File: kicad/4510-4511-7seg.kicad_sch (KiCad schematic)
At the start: 14 parts, among them U13 4029, U14 4511, U15 TDSR-3163-G

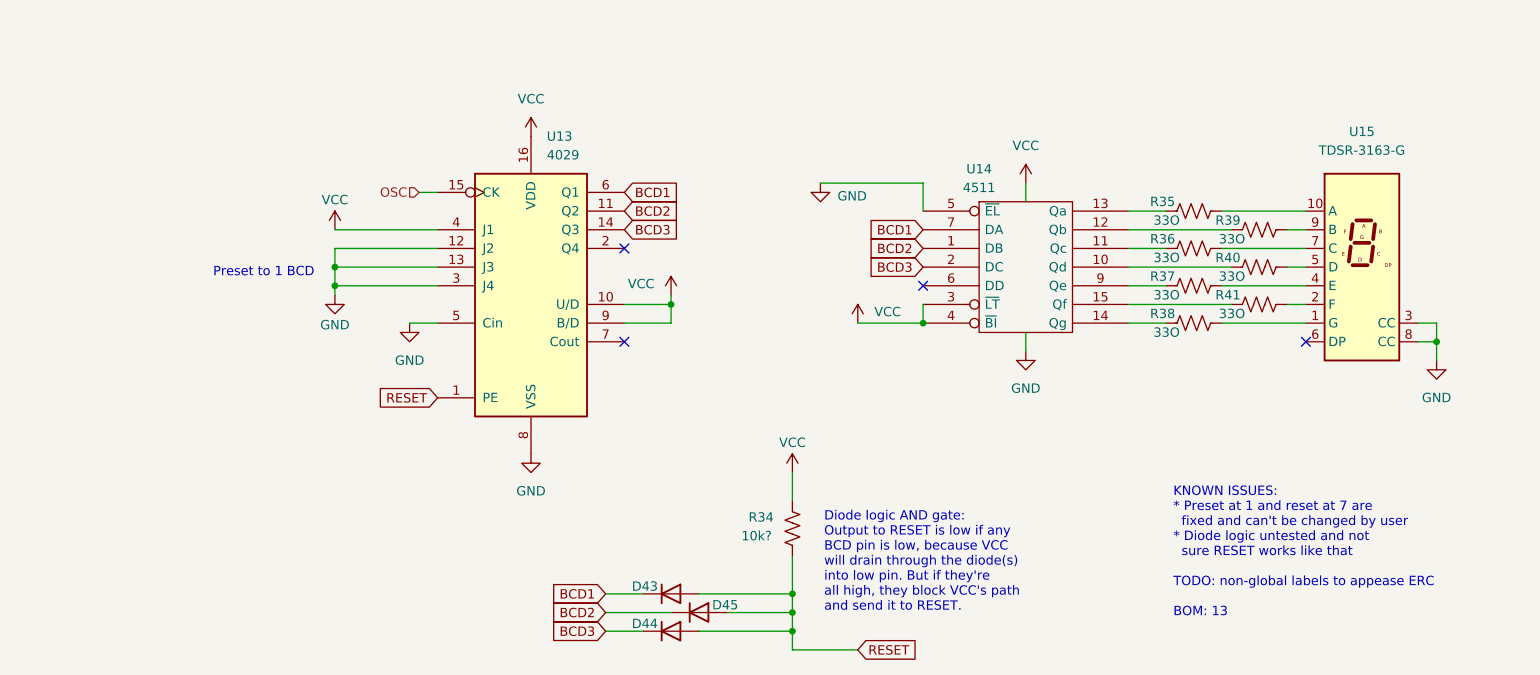
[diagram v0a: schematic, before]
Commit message: Add CD4510 to CD4511 to 7seg schematic
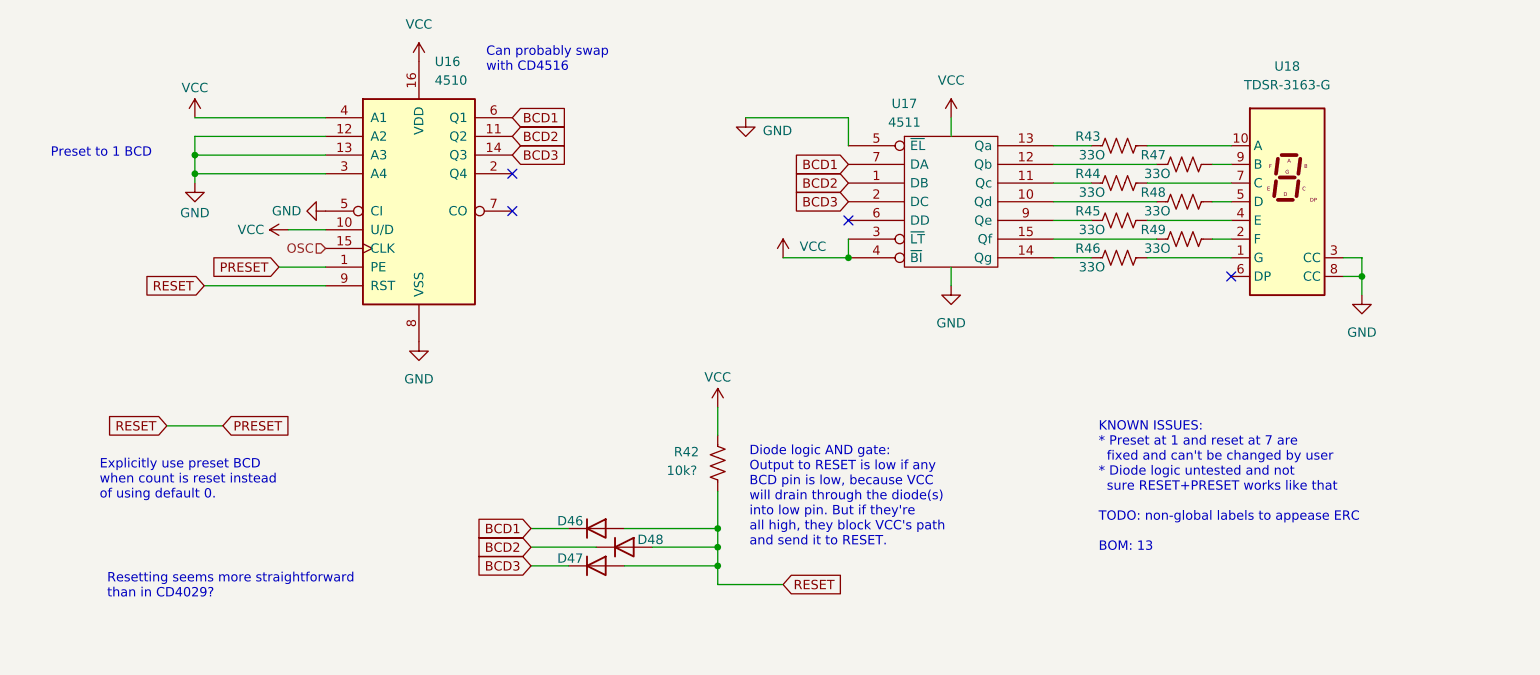
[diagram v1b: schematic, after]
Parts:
- removed D43, D44, D45: 1N4148WT, Diode_SMD:D_SOD-523, symbol Diode:1N4148WT
- removed R34: 10k?, Resistor_THT:R_Axial_DIN0204_L3.6mm_D1.6mm_P7.62mm_Horizontal, symbol Device:R_US
- removed R35, R36, R37, R38, R39, R40, R41: 33O, Resistor_THT:R_Axial_DIN0204_L3.6mm_D1.6mm_P7.62mm_Horizontal, symbol Device:R_US
- removed U13: 4029, symbol 4xxx:4029
- removed U14: 4511, symbol 4xxx_IEEE:4511
- removed U15: TDSR-3163-G, symbol parts_cafe:TDSR-3163-G
- added D46, D47, D48: 1N4148WT, Diode_SMD:D_SOD-523, symbol Diode:1N4148WT
- added R42: 10k?, Resistor_THT:R_Axial_DIN0204_L3.6mm_D1.6mm_P7.62mm_Horizontal, symbol Device:R_US
- added R43, R44, R45, R46, R47, R48, R49: 33O, Resistor_THT:R_Axial_DIN0204_L3.6mm_D1.6mm_P7.62mm_Horizontal, symbol Device:R_US
- added U16: 4510, symbol 4xxx:4510
- added U17: 4511, symbol 4xxx_IEEE:4511
- added U18: TDSR-3163-G, symbol parts_cafe:TDSR-3163-G
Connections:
- net BCD1: now also D46.1 (K), U16.6 (Q1), U17.7 (DA)
- net BCD2: now also D48.1 (K), U16.11 (Q2), U17.1 (DB)
- net BCD3: now also D47.1 (K), U16.14 (Q3), U17.2 (DC)
- net GND: now also U16.12 (A2), U16.13 (A3), U16.3 (A4), U16.5 (CI), U16.8 (VSS), U17.5 (~{EL}), U17.8 (Vss), U18.3 (CC), U18.8 (CC)
- net OSC: now also U16.15 (CLK)
- net VCC: now also R42.2, U16.10 (U/D), U16.16 (VDD), U16.4 (A1), U17.16 (Vdd), U17.3 (~{LT}), U17.4 (~{BI})
- new net: R48.1, U17.10 (Qd)
- new net: R48.2, U18.5 (D)
- new net: R46.2, U18.1 (G)
- new net: R43.2, U18.10 (A)
- new net: R49.2, U18.2 (F)
- new net: R45.2, U18.4 (E)
- new net: R44.2, U18.7 (C)
- new net: R47.2, U18.9 (B)
- new net: R44.1, U17.11 (Qc)
- new net: R47.1, U17.12 (Qb)
- new net: R43.1, U17.13 (Qa)
- new net: R46.1, U17.14 (Qg)
- new net: R49.1, U17.15 (Qf)
- new net: R45.1, U17.9 (Qe)
- new net PRESET: D46.2 (A), D47.2 (A), D48.2 (A), R42.1, U16.1 (PE), U16.9 (RST)
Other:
- note added: "Can probably swap with CD4516"
- note added: "Explicitly use preset BCD when count is reset instead of using default 0."
- note added: "KNOWN ISSUES: * Preset at 1 and reset at 7 are fixed and can't be changed by user * Diode logic untested and not sure RESET+PRESET works like that TODO: non-global labels to appease ERC BOM: 13"
- note added: "Resetting seems more straightforward than in CD4029?"
- note removed: "KNOWN ISSUES: * Preset at 1 and reset at 7 are fixed and can't be changed by user * Diode logic untested and not sure RESET works like that TODO: non-global labels to appease ERC BOM: 13"

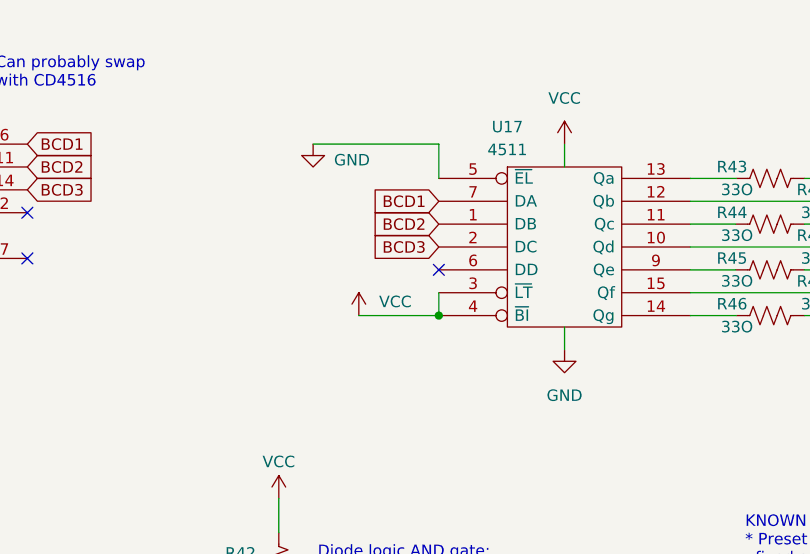
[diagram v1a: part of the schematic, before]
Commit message: Fix missing 4511 BCD pin
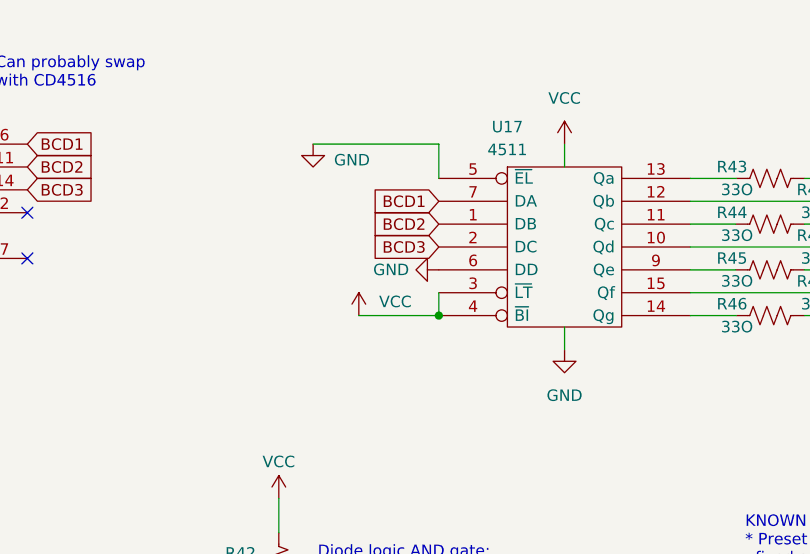
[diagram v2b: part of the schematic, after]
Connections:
- net GND: now also U17.6 (DD)
- no-connect marks 4 -> 3
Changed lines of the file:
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@@
-	)
-	(no_connect
-		(at 154.94 86.36)
 	)
 	(no_connect
@@
 					(unit 1)
 				)
+			)
+		)
+	)
+	(symbol
+		(lib_name "GND_1")
+		(lib_id "power:GND")
+		(at 154.94 86.36 270)
+		(unit 1)
+		(exclude_from_sim no)
+		(in_bom yes)
+		(on_board yes)
+		(dnp no)
+		(property "Reference" "#PWR064"
+			(at 148.59 86.36 0)
+			(effects
+				(font
+					(size 1.27 1.27)
+				)
+				(hide yes)
+			)
+		)
+		(property "Value" "GND"
+			(at 151.638 86.36 90)
+			(effects
+				(font
+					(size 1.27 1.27)
+				)
+				(justify right)
+			)
+		)
+		(property "Footprint" ""
+			(at 154.94 86.36 0)
+			(effects
+				(font
+					(size 1.27 1.27)
+				)
+				(hide yes)
+			)
+		)
+		(property "Datasheet" ""
+			(at 154.94 86.36 0)
+			(effects
+				(font
+					(size 1.27 1.27)
+				)
+				(hide yes)
+			)
+		)
+		(property "Description" "Power symbol creates a global label with name \"GND\" , ground"
+			(at 154.94 86.36 0)
+			(effects
+				(font
+					(size 1.27 1.27)
+				)
+				(hide yes)
+			)
+		)
+		(pin "1"
+		)
+		(instances
+			(project "space_dice"
+				(path "/bcd0d850-a20d-42e1-b97f-b14f9222717c/bf281fbb-b458-46c0-8938-ced8826deda0"
+					(reference "#PWR064")
+					(unit 1)
+				)

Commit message: It works! Finalize 4510-4511-7seg
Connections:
- net GND: now also U16.9 (RST); no longer U17.6 (DD)
- net BCD4: now reaches U16.2 (Q4)
- net BCD4: now also U17.6 (DD)
- net PRESET renamed LOAD
- net LOAD: no longer U16.9 (RST)
- no-connect marks 3 -> 2
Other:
- note added: "BCD4 will always be 0 but it can't hurt to connect them instead of using GND"
- note added: "Diode logic AND gate: Output is low if any BCD pin is low, because VCC will drain through the diode(s) into low pin. But if they're all high, they block VCC's path and send it to output."
- note added: "KNOWN ISSUES: * Preset at 1 and reset at 7 are fixed and can't be changed by user TODO: non-global labels to appease ERC BOM: 14"
- note removed: "Diode logic AND gate: Output to RESET is low if any BCD pin is low, because VCC will drain through the diode(s) into low pin. But if they're all high, they block VCC's path and send it to RESET."
- note removed: "Explicitly use preset BCD when count is reset instead of using default 0."
- note removed: "KNOWN ISSUES: * Preset at 1 and reset at 7 are fixed and can't be changed by user * Diode logic untested and not sure RESET+PRESET works like that TODO: non-global labels to appease ERC BOM: 13"
- note removed: "Resetting seems more straightforward than in CD4029?"
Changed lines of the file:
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@@
 	(generator_version "9.0")
 	(paper "A4")
-	(text "Diode logic AND gate:\nOutput to RESET is low if any\nBCD pin is low, because VCC\nwill drain through the diode(s)\ninto low pin. But if they're\nall high, they block VCC's path\nand send it to RESET."
+	(text "Diode logic AND gate:\nOutput is low if any\nBCD pin is low, because VCC\nwill drain through the diode(s)\ninto low pin. But if they're\nall high, they block VCC's path\nand send it to output."
 		(exclude_from_sim no)
 		(at 141.478 123.952 0)
@@
 		)
 	)
-	(text "KNOWN ISSUES:\n* Preset at 1 and reset at 7 are\n  fixed and can't be changed by user\n* Diode logic untested and not\n  sure RESET+PRESET works like that\n\nTODO: non-global labels to appease ERC\n\nBOM: 13"
+	(text "BCD4 will always be 0\nbut it can't hurt to\nconnect them instead\nof using GND"
+		(exclude_from_sim no)
+		(at 118.11 87.376 0)
+		(effects
+			(font
+				(size 1.27 1.27)
+			)
+			(justify left)
+		)
+	)
+	(text "KNOWN ISSUES:\n* Preset at 1 and reset at 7 are\n  fixed and can't be changed by user\n\nTODO: non-global labels to appease ERC\n\nBOM: 14"
 		(exclude_from_sim no)
 		(at 188.976 131.572 0)
@@
 		)
 	)
-	(text "Resetting seems more straightforward\nthan in CD4029?"
-		(exclude_from_sim no)
-		(at 54.102 136.144 0)
-		(effects
-			(font
-				(size 1.27 1.27)
-			)
-			(justify left)
-		)
-	)
 	(text "Preset to 1 BCD"
 		(exclude_from_sim no)
@@
 		)
 	)
-	(text "Explicitly use preset BCD\nwhen count is reset instead\nof using default 0."
-		(exclude_from_sim no)
-		(at 53.086 121.666 0)
-		(effects
-			(font
-				(size 1.27 1.27)
-			)
-			(justify left)
-		)
-	)
 	(text "Can probably swap\nwith CD4516"
 		(exclude_from_sim no)
@@
 	)
 	(no_connect
-		(at 109.22 80.01)
-	)
-	(no_connect
 		(at 109.22 85.09)
 	)
@@
 	(wire
 		(pts
-			(xy 62.23 114.3) (xy 69.85 114.3)
-		)
-		(stroke
-			(width 0)
-			(type default)
-		)
-	)
-	(wire
-		(pts
 			(xy 66.04 77.47) (xy 83.82 77.47)
 		)
@@
 	(wire
 		(pts
-			(xy 67.31 95.25) (xy 83.82 95.25)
-		)
-		(stroke
-			(width 0)
-			(type default)
-		)
-	)
-	(wire
-		(pts
 			(xy 140.97 72.39) (xy 154.94 72.39)
 		)
@@
 			(width 0)
 			(type default)
+		)
+	)
+	(global_label "LOAD"
+		(shape input)
+		(at 146.05 135.89 0)
+		(fields_autoplaced yes)
+		(effects
+			(font
+				(size 1.27 1.27)
+			)
+			(justify left)
+		)
+		(property "Intersheetrefs" "${INTERSHEET_REFS}"
+			(at 153.7524 135.89 0)
+			(effects
+				(font
+					(size 1.27 1.27)
+				)
+				(justify left)
+				(hide yes)
+			)
 		)
 	)
@@
 		)
 	)
-	(global_label "PRESET"
+	(global_label "LOAD"
 		(shape input)
 		(at 77.47 92.71 180)
@@
 		)
 		(property "Intersheetrefs" "${INTERSHEET_REFS}"
-			(at 67.4697 92.71 0)
+			(at 69.7676 92.71 0)
 			(effects
 				(font
@@
 		)
 	)
-	(global_label "RESET"
-		(shape input)
-		(at 146.05 135.89 0)
-		(fields_autoplaced yes)
-		(effects
-			(font
-				(size 1.27 1.27)
-			)
-			(justify left)
-		)
-		(property "Intersheetrefs" "${INTERSHEET_REFS}"
-			(at 154.7803 135.89 0)
-			(effects
-				(font
-					(size 1.27 1.27)
-				)
-				(justify left)
-				(hide yes)
-			)
-		)
-	)
 	(global_label "BCD3"
 		(shape input)
@@
 		)
 	)
-	(global_label "RESET"
+	(global_label "BCD4"
 		(shape input)
-		(at 62.23 114.3 180)
+		(at 154.94 86.36 180)
 		(fields_autoplaced yes)
 		(effects
@@
 		)
 		(property "Intersheetrefs" "${INTERSHEET_REFS}"
-			(at 53.4997 114.3 0)
-			(effects
-				(font
-					(size 1.27 1.27)
-				)
-				(justify right)
-				(hide yes)
-			)
-		)
-	)
-	(global_label "RESET"
-		(shape input)
-		(at 67.31 95.25 180)
-		(fields_autoplaced yes)
-		(effects
-			(font
-				(size 1.27 1.27)
-			)
-			(justify right)
-		)
-		(property "Intersheetrefs" "${INTERSHEET_REFS}"
-			(at 58.5797 95.25 0)
+			(at 146.9353 86.36 0)
 			(effects
 				(font
@@
 		)
 	)
-	(global_label "PRESET"
-		(shape input)
-		(at 69.85 114.3 0)
-		(fields_autoplaced yes)
-		(effects
-			(font
-				(size 1.27 1.27)
-			)
-			(justify left)
-		)
-		(property "Intersheetrefs" "${INTERSHEET_REFS}"
-			(at 79.8503 114.3 0)
-			(effects
-				(font
-					(size 1.27 1.27)
-				)
-				(justify left)
-				(hide yes)
-			)
-		)
-	)
 	(global_label "BCD1"
 		(shape input)
@@
 		)
 	)
+	(global_label "BCD4"
+		(shape input)
+		(at 109.22 80.01 0)
+		(fields_autoplaced yes)
+		(effects
+			(font
+				(size 1.27 1.27)
+			)
+			(justify left)
+		)
+		(property "Intersheetrefs" "${INTERSHEET_REFS}"
+			(at 117.2247 80.01 0)
+			(effects
+				(font
+					(size 1.27 1.27)
+				)
+				(justify left)
+				(hide yes)
+			)
+		)
+	)
 	(hierarchical_label "OSC"
 		(shape input)
@@
 	)
 	(symbol
-		(lib_name "GND_1")
-		(lib_id "power:GND")
-		(at 154.94 86.36 270)
-		(unit 1)
-		(exclude_from_sim no)
-		(in_bom yes)
-		(on_board yes)
-		(dnp no)
-		(property "Reference" "#PWR064"
-			(at 148.59 86.36 0)
-			(effects
-				(font
-					(size 1.27 1.27)
-				)
-				(hide yes)
-			)
-		)
-		(property "Value" "GND"
-			(at 151.638 86.36 90)
-			(effects
-				(font
-					(size 1.27 1.27)
-				)
-				(justify right)
-			)
-		)
-		(property "Footprint" ""
-			(at 154.94 86.36 0)
-			(effects
-				(font
-					(size 1.27 1.27)
-				)
-				(hide yes)
-			)
-		)
-		(property "Datasheet" ""
-			(at 154.94 86.36 0)
-			(effects
-				(font
-					(size 1.27 1.27)
-				)
-				(hide yes)
-			)
-		)
-		(property "Description" "Power symbol creates a global label with name \"GND\" , ground"
-			(at 154.94 86.36 0)
-			(effects
-				(font
-					(size 1.27 1.27)
-				)
-				(hide yes)
-			)
-		)
-		(pin "1"
-		)
-		(instances
-			(project "space_dice"
-				(path "/bcd0d850-a20d-42e1-b97f-b14f9222717c/bf281fbb-b458-46c0-8938-ced8826deda0"
-					(reference "#PWR064")
-					(unit 1)
-				)
-			)
-		)
-	)
-	(symbol
 		(lib_name "VCC_1")
 		(lib_id "power:VCC")
@@
 					(unit 1)
 				)
+			)
+		)
+	)
+	(symbol
+		(lib_name "GND_1")
+		(lib_id "power:GND")
+		(at 83.82 95.25 270)
+		(unit 1)
+		(exclude_from_sim no)
+		(in_bom yes)
+		(on_board yes)
+		(dnp no)
+		(property "Reference" "#PWR067"
+			(at 77.47 95.25 0)
+			(effects
+				(font
+					(size 1.27 1.27)
+				)
+				(hide yes)
+			)
+		)
+		(property "Value" "GND"
+			(at 80.518 95.25 90)
+			(effects
+				(font
+					(size 1.27 1.27)
+				)
+				(justify right)
+			)
+		)
+		(property "Footprint" ""
+			(at 83.82 95.25 0)
+			(effects
+				(font
+					(size 1.27 1.27)
+				)
+				(hide yes)
+			)
+		)
+		(property "Datasheet" ""
+			(at 83.82 95.25 0)
+			(effects
+				(font
+					(size 1.27 1.27)
+				)
+				(hide yes)
+			)
+		)
+		(property "Description" "Power symbol creates a global label with name \"GND\" , ground"
+			(at 83.82 95.25 0)
+			(effects
+				(font
+					(size 1.27 1.27)
+				)
+				(hide yes)
+			)
+		)
+		(pin "1"
+		)
+		(instances
+			(project "space_dice"
+				(path "/bcd0d850-a20d-42e1-b97f-b14f9222717c/bf281fbb-b458-46c0-8938-ced8826deda0"
+					(reference "#PWR067")
+					(unit 1)
+				)
